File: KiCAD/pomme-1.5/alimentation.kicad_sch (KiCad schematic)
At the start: 0 parts

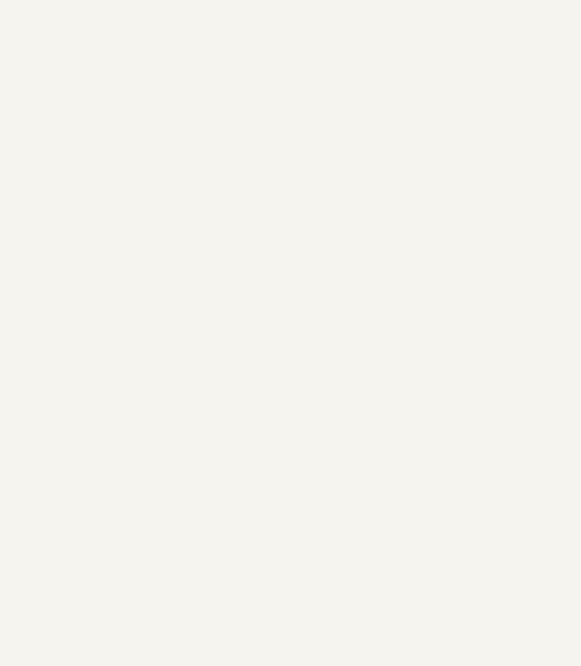
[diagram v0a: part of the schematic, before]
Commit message: Modification de test1.s et de la schématique. L'ordinateur fonctionne à 3.68Mhz
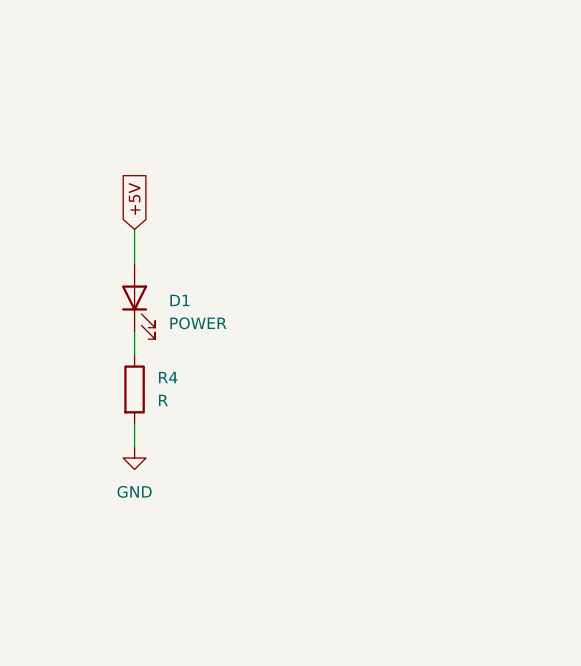
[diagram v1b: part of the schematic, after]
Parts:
- added D1: POWER, symbol Device:LED
- added R4: R, symbol Device:R
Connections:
- new net: D1.1 (K), R4.1
- new net +5V: D1.2 (A)
- new net GND: R4.2

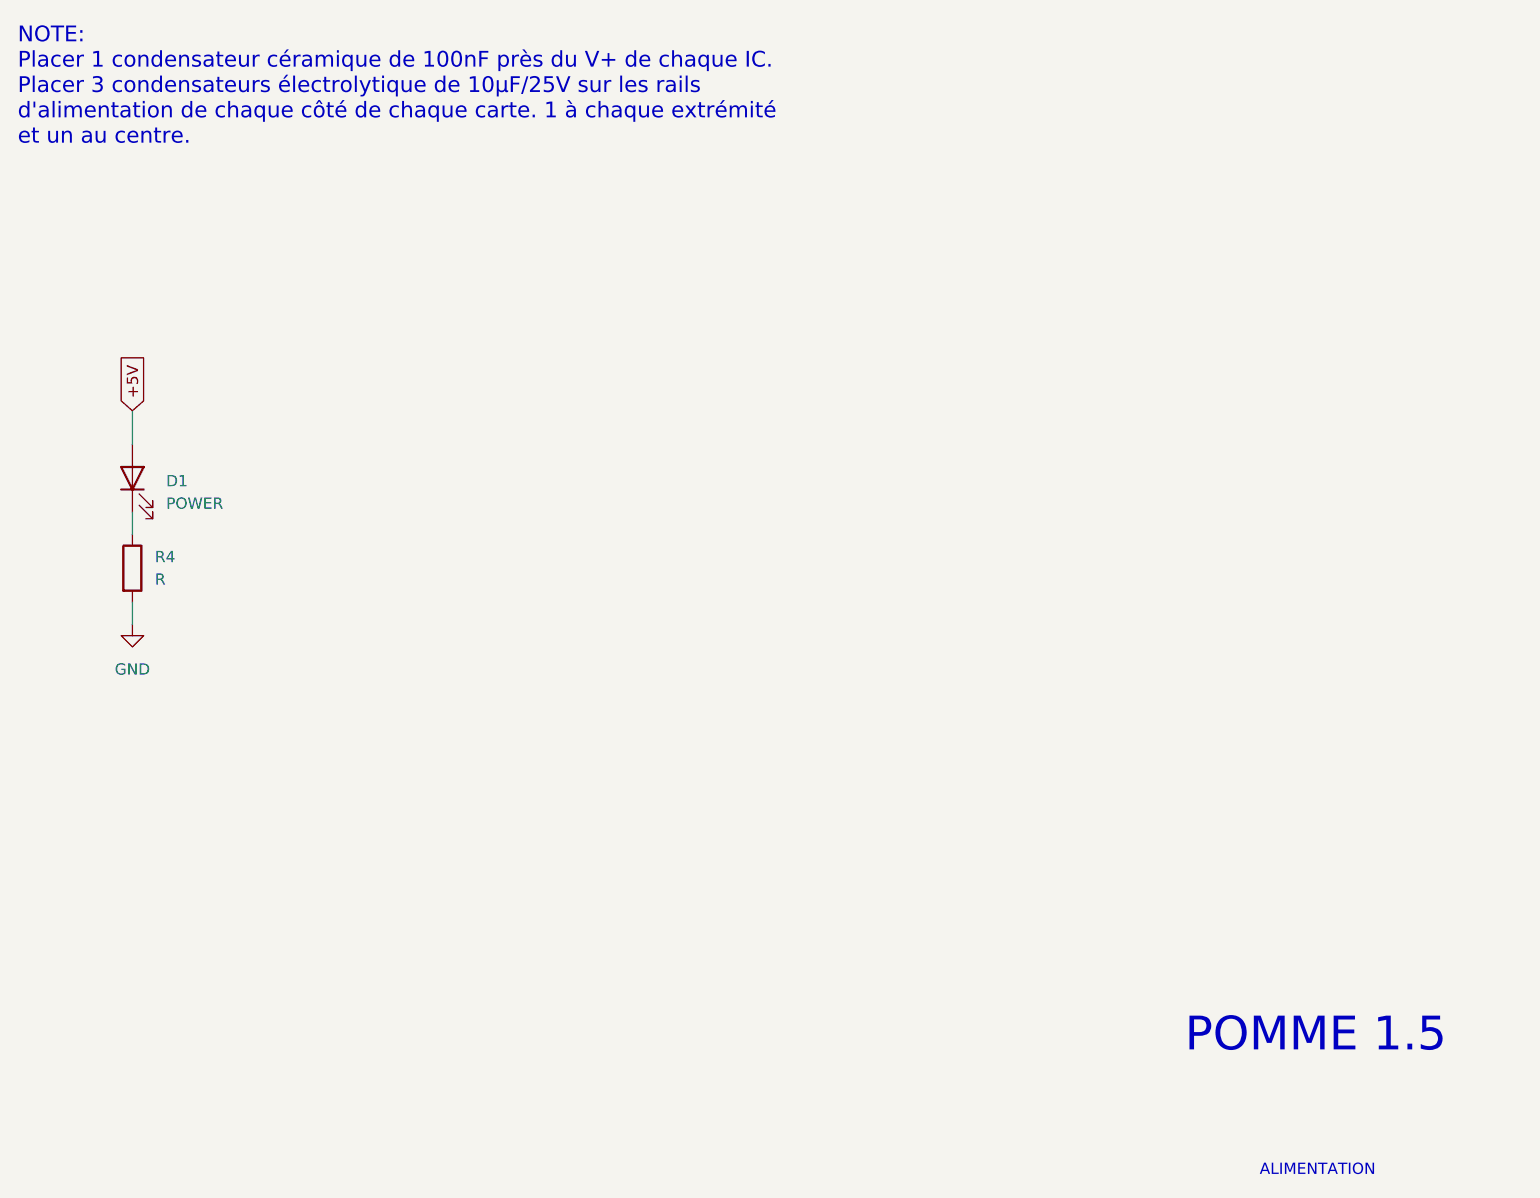
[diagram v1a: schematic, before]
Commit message: Complété schématique alimentation
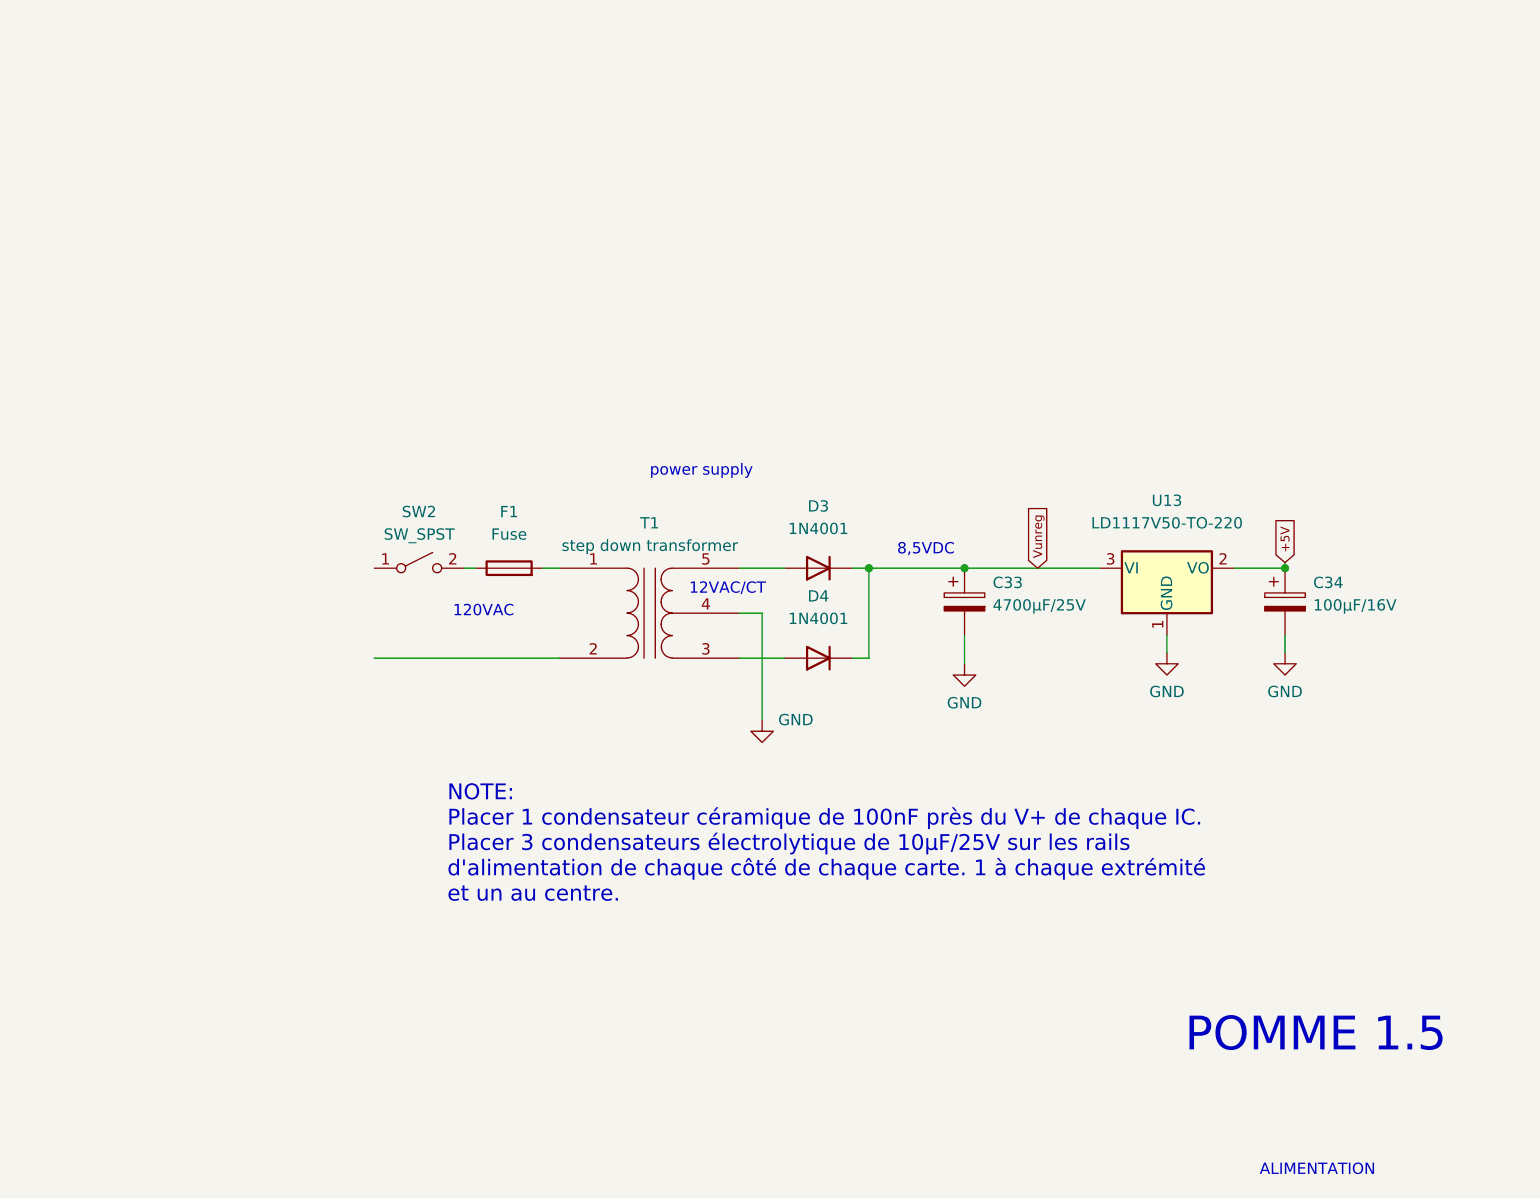
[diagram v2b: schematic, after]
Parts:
- removed D1: POWER, symbol Device:LED
- removed R4: R, symbol Device:R
- added C33: 4700µF/25V, symbol Device:C_Polarized
- added C34: 100µF/16V, symbol Device:C_Polarized
- added D3, D4: 1N4001, Diode_THT:D_DO-41_SOD81_P10.16mm_Horizontal, symbol Diode:1N4004
- added F1: Fuse, symbol Device:Fuse
- added SW2: SW_SPST, symbol Switch:SW_SPST
- added T1: step down transformer, symbol Device:Transformer_1P_SS
- added U13: LD1117V50-TO-220, Package_TO_SOT_SMD:SOT-223-3_TabPin2, symbol Regulator_Linear:LD1117S12TR_SOT223
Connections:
- net +5V: now also C34.1, U13.2 (VO)
- net GND: now also C33.2, C34.2, T1.4 (SC), U13.1 (GND)
- new net: F1.1, SW2.2 (B)
- new net: F1.2, T1.1 (AA)
- new net: D3.2 (A), T1.5 (SB)
- new net: D4.2 (A), T1.3 (SA)
- new net Vunreg: C33.1, D3.1 (K), D4.1 (K), U13.3 (VI)
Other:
- note added: "120VAC"
- note added: "12VAC/CT"
- note added: "8,5VDC"
- note added: "power supply"

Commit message: Correction schematique
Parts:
- F1: value Fuse -> 1/4 A
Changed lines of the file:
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@@
 			)
 		)
-		(property "Value" "Fuse"
+		(property "Value" "1/4 A"
 			(at 102.235 118.11 90)
 			(effects
@@
 				)
 			)
+			(project "alimentation"
+				(path "/62504db6-7d57-4226-a69c-802abd89335e"
+					(reference "F1")
+					(unit 1)
+				)
+			)
 		)
 	)
@@
 				)
 			)
+			(project "alimentation"
+				(path "/62504db6-7d57-4226-a69c-802abd89335e"
+					(reference "D1")
+					(unit 1)
+				)
+			)
 		)
 	)
@@
 				)
 			)
+			(project "alimentation"
+				(path "/62504db6-7d57-4226-a69c-802abd89335e"
+					(reference "SW1")
+					(unit 1)
+				)
+			)
 		)
 	)
@@
 				)
 			)
+			(project "alimentation"
+				(path "/62504db6-7d57-4226-a69c-802abd89335e"
+					(reference "T1")
+					(unit 1)
+				)
+			)
 		)
 	)
@@
 				)
 			)
+			(project "alimentation"
+				(path "/62504db6-7d57-4226-a69c-802abd89335e"
+					(reference "U1")
+					(unit 1)
+				)
+			)
 		)
 	)
@@
 				)
 			)
+			(project "alimentation"
+				(path "/62504db6-7d57-4226-a69c-802abd89335e"
+					(reference "#PWR04")
+					(unit 1)
+				)
+			)
 		)
 	)
@@
 				)
 			)
+			(project "alimentation"
+				(path "/62504db6-7d57-4226-a69c-802abd89335e"
+					(reference "C2")
+					(unit 1)
+				)
+			)
 		)
 	)
@@
 				)
 			)
+			(project "alimentation"
+				(path "/62504db6-7d57-4226-a69c-802abd89335e"
+					(reference "#PWR03")
+					(unit 1)
+				)
+			)
 		)
 	)
@@
 				)
 			)
+			(project "alimentation"
+				(path "/62504db6-7d57-4226-a69c-802abd89335e"
+					(reference "C1")
+					(unit 1)
+				)
+			)
 		)
 	)
@@
 				)
 			)
+			(project "alimentation"
+				(path "/62504db6-7d57-4226-a69c-802abd89335e"
+					(reference "#PWR02")
+					(unit 1)
+				)
+			)
 		)
 	)
@@
 				)
 			)
+			(project "alimentation"
+				(path "/62504db6-7d57-4226-a69c-802abd89335e"
+					(reference "#PWR01")
+					(unit 1)
+				)
+			)
 		)
 	)
@@
 				)
 			)
-		)
-	)
+			(project "alimentation"
+				(path "/62504db6-7d57-4226-a69c-802abd89335e"
+					(reference "D2")
+					(unit 1)
+				)
+			)
+		)
+	)
+	(sheet_instances
+		(path "/"
+			(page "1")
+		)
+	)
